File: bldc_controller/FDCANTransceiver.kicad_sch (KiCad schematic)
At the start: 4 parts, among them U4 TCAN1057AEVDRQ1

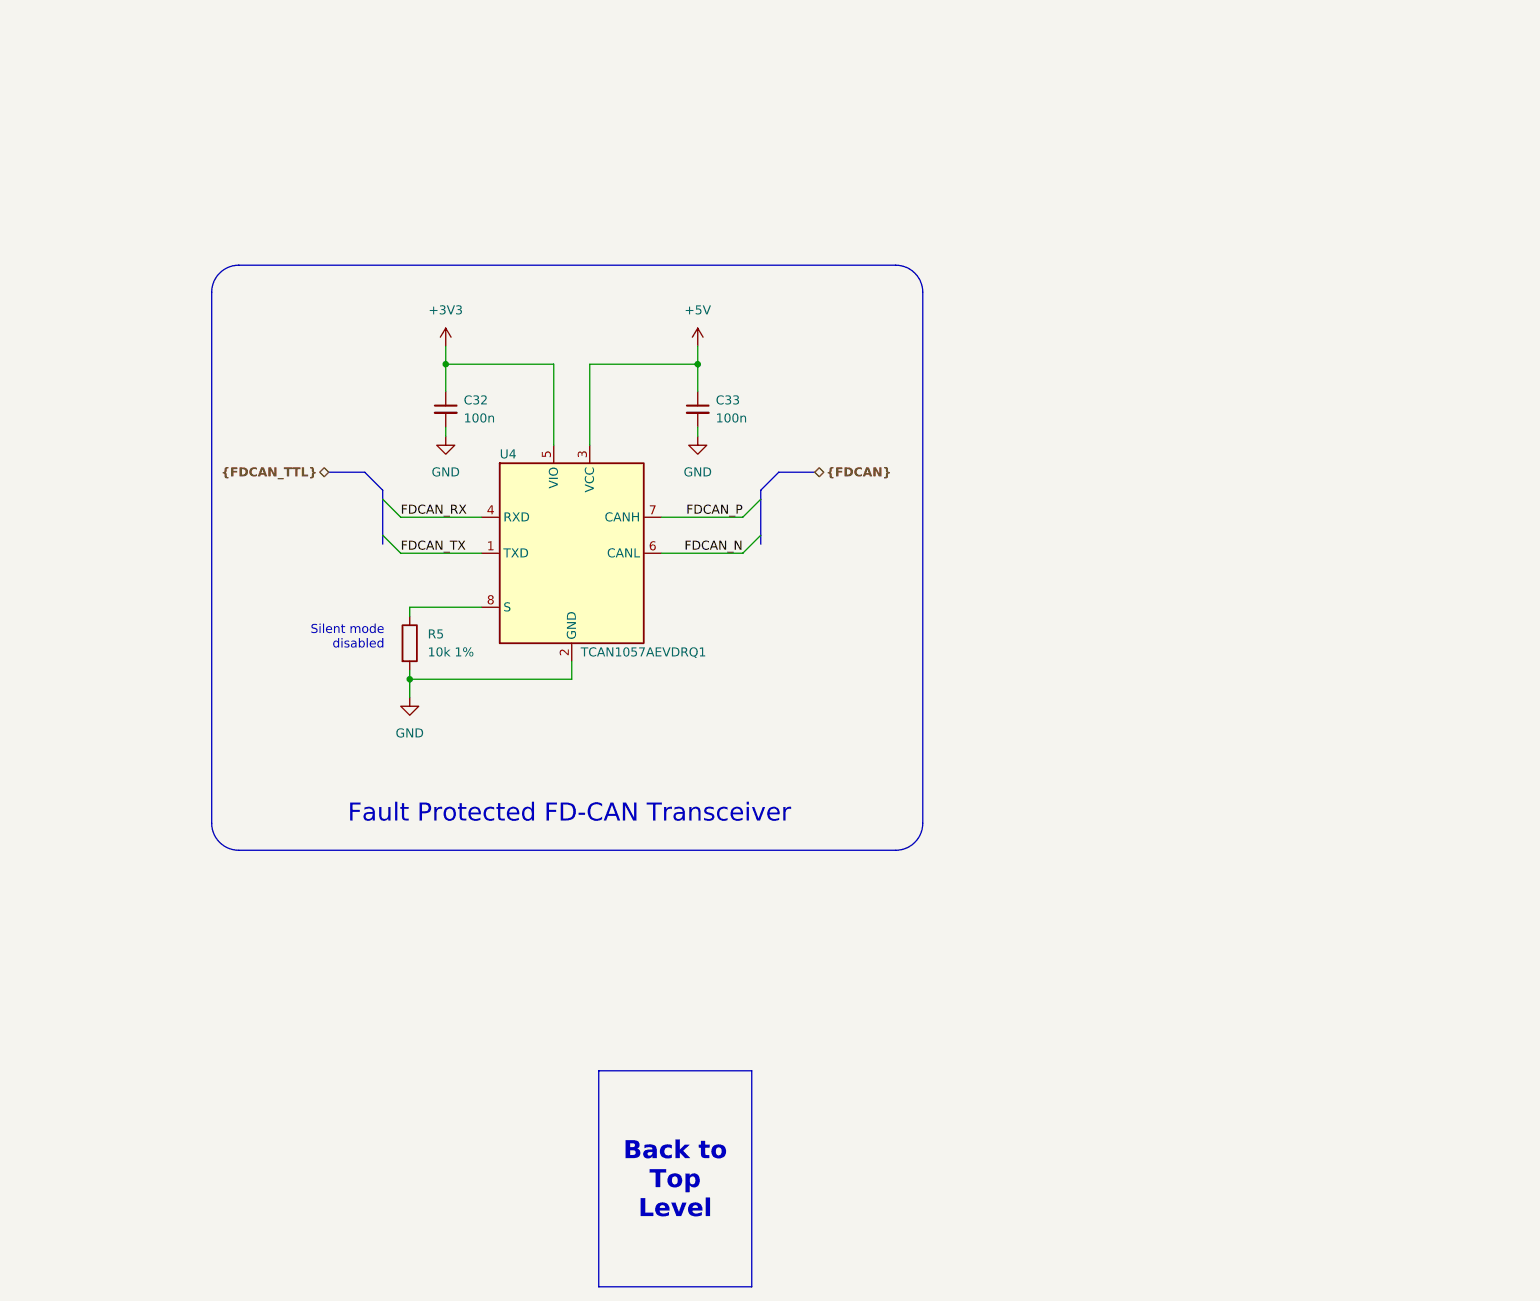
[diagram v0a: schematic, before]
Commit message: added temporary footprints and deleted extra files
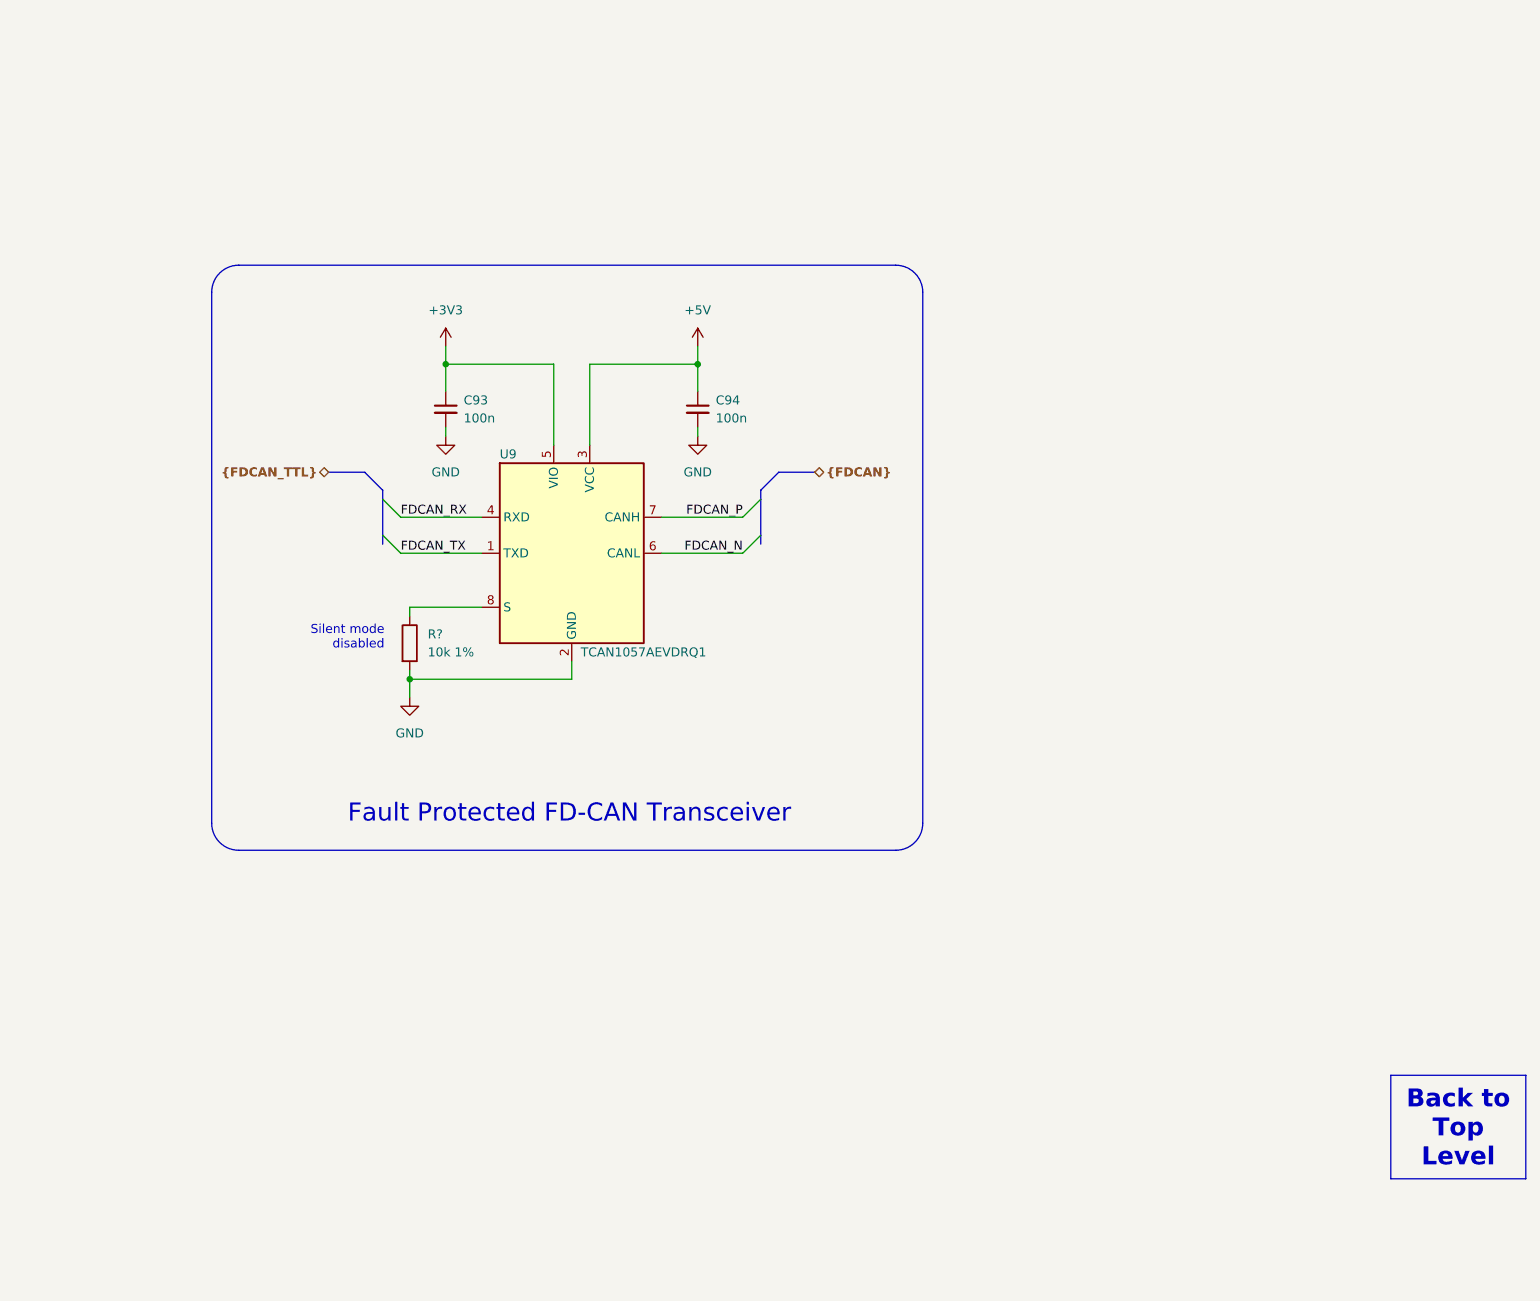
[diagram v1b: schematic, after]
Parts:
- C93: renamed from C32; footprint (none) -> Capacitor_SMD:C_0402_1005Metric
- C94: renamed from C33; footprint (none) -> Capacitor_SMD:C_0402_1005Metric
- R?: renamed from R5; footprint (none) -> Resistor_SMD:R_0402_1005Metric
- renumbered U4 to U9
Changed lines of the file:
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@@
   )
   (text_box "Back to Top Level"
-    (at 153.67 165.735 0) (size 21.59 30.48)
+    (at 265.43 166.37 0) (size 19.05 14.605)
     (stroke (width 0) (type default) (color 0 0 0 1))
     (fill (type color) (color 0 0 0 0.1))
@@
   (symbol (lib_id "power:+3V3") (at 132.08 63.5 0) (unit 1)
     (in_bom yes) (on_board yes) (dnp no) (fields_autoplaced)
-    (property "Reference" "#PWR043" (at 132.08 67.31 0)
+    (property "Reference" "#PWR054" (at 132.08 67.31 0)
       (effects (font (size 1.27 1.27)) hide)
     )
@@
       (project "bldc_controller"
         (path "/0650c7a8-acba-429c-9f8e-eec0baf0bc1c/926acdff-90be-4f7b-9e19-9f96ee9f0571"
-          (reference "#PWR043") (unit 1)
+          (reference "#PWR054") (unit 1)
         )
       )
@@
   (symbol (lib_id "power:GND") (at 127 113.03 0) (unit 1)
     (in_bom yes) (on_board yes) (dnp no) (fields_autoplaced)
-    (property "Reference" "#PWR042" (at 127 119.38 0)
+    (property "Reference" "#PWR053" (at 127 119.38 0)
       (effects (font (size 1.27 1.27)) hide)
     )
@@
       (project "bldc_controller"
         (path "/0650c7a8-acba-429c-9f8e-eec0baf0bc1c/926acdff-90be-4f7b-9e19-9f96ee9f0571"
-          (reference "#PWR042") (unit 1)
+          (reference "#PWR053") (unit 1)
         )
       )
@@
   (symbol (lib_id "power:GND") (at 132.08 76.2 0) (unit 1)
     (in_bom yes) (on_board yes) (dnp no) (fields_autoplaced)
-    (property "Reference" "#PWR044" (at 132.08 82.55 0)
+    (property "Reference" "#PWR055" (at 132.08 82.55 0)
       (effects (font (size 1.27 1.27)) hide)
     )
@@
       (project "bldc_controller"
         (path "/0650c7a8-acba-429c-9f8e-eec0baf0bc1c/926acdff-90be-4f7b-9e19-9f96ee9f0571"
-          (reference "#PWR044") (unit 1)
+          (reference "#PWR055") (unit 1)
         )
       )
@@
   (symbol (lib_id "power:GND") (at 167.64 76.2 0) (mirror y) (unit 1)
     (in_bom yes) (on_board yes) (dnp no) (fields_autoplaced)
-    (property "Reference" "#PWR046" (at 167.64 82.55 0)
+    (property "Reference" "#PWR057" (at 167.64 82.55 0)
       (effects (font (size 1.27 1.27)) hide)
     )
@@
       (project "bldc_controller"
         (path "/0650c7a8-acba-429c-9f8e-eec0baf0bc1c/926acdff-90be-4f7b-9e19-9f96ee9f0571"
-          (reference "#PWR046") (unit 1)
+          (reference "#PWR057") (unit 1)
         )
       )
@@
   (symbol (lib_id "Device:C_Small") (at 167.64 72.39 0) (unit 1)
     (in_bom yes) (on_board yes) (dnp no)
-    (property "Reference" "C33" (at 170.18 71.1263 0)
+    (property "Reference" "C94" (at 170.18 71.1263 0)
       (effects (font (size 1.27 1.27)) (justify left))
     )
@@
       (effects (font (size 1.27 1.27)) (justify left))
     )
-    (property "Footprint" "" (at 167.64 72.39 0)
+    (property "Footprint" "Capacitor_SMD:C_0402_1005Metric" (at 167.64 72.39 0)
       (effects (font (size 1.27 1.27)) hide)
     )
@@
       (project "bldc_controller"
         (path "/0650c7a8-acba-429c-9f8e-eec0baf0bc1c/926acdff-90be-4f7b-9e19-9f96ee9f0571"
-          (reference "C33") (unit 1)
+          (reference "C94") (unit 1)
         )
       )
@@
   (symbol (lib_id "power:+5V") (at 167.64 63.5 0) (unit 1)
     (in_bom yes) (on_board yes) (dnp no) (fields_autoplaced)
-    (property "Reference" "#PWR045" (at 167.64 67.31 0)
+    (property "Reference" "#PWR056" (at 167.64 67.31 0)
       (effects (font (size 1.27 1.27)) hide)
     )
@@
       (project "bldc_controller"
         (path "/0650c7a8-acba-429c-9f8e-eec0baf0bc1c/926acdff-90be-4f7b-9e19-9f96ee9f0571"
-          (reference "#PWR045") (unit 1)
+          (reference "#PWR056") (unit 1)
         )
       )
@@
   (symbol (lib_id "0_transceiver:TCAN1057AEVDRQ1") (at 149.86 92.71 0) (unit 1)
     (in_bom yes) (on_board yes) (dnp no)
-    (property "Reference" "U4" (at 139.7 78.74 0)
+    (property "Reference" "U9" (at 139.7 78.74 0)
       (effects (font (size 1.27 1.27)) (justify left))
     )
@@
       (project "bldc_controller"
         (path "/0650c7a8-acba-429c-9f8e-eec0baf0bc1c/926acdff-90be-4f7b-9e19-9f96ee9f0571"
-          (reference "U4") (unit 1)
+          (reference "U9") (unit 1)
         )
       )
@@
   (symbol (lib_id "Device:C_Small") (at 132.08 72.39 0) (unit 1)
     (in_bom yes) (on_board yes) (dnp no) (fields_autoplaced)
-    (property "Reference" "C32" (at 134.62 71.1263 0)
+    (property "Reference" "C93" (at 134.62 71.1263 0)
       (effects (font (size 1.27 1.27)) (justify left))
     )
@@
       (effects (font (size 1.27 1.27)) (justify left))
     )
-    (property "Footprint" "" (at 132.08 72.39 0)
+    (property "Footprint" "Capacitor_SMD:C_0402_1005Metric" (at 132.08 72.39 0)
       (effects (font (size 1.27 1.27)) hide)
     )
@@
       (project "bldc_controller"
         (path "/0650c7a8-acba-429c-9f8e-eec0baf0bc1c/926acdff-90be-4f7b-9e19-9f96ee9f0571"
-          (reference "C32") (unit 1)
+          (reference "C93") (unit 1)
         )
       )
@@
   (symbol (lib_id "Device:R") (at 127 105.41 0) (unit 1)
     (in_bom yes) (on_board yes) (dnp no) (fields_autoplaced)
-    (property "Reference" "R5" (at 129.54 104.14 0)
+    (property "Reference" "R?" (at 129.54 104.14 0)
       (effects (font (size 1.27 1.27)) (justify left))
     )
@@
       (effects (font (size 1.27 1.27)) (justify left))
     )
-    (property "Footprint" "" (at 125.222 105.41 90)
+    (property "Footprint" "Resistor_SMD:R_0402_1005Metric" (at 125.222 105.41 90)
       (effects (font (size 1.27 1.27)) hide)
     )
@@
       (project "bldc_controller"
         (path "/0650c7a8-acba-429c-9f8e-eec0baf0bc1c/ce1ea51b-4118-4fb5-9a41-40670da86eb7"
-          (reference "R5") (unit 1)
-        )
-        (path "/0650c7a8-acba-429c-9f8e-eec0baf0bc1c/926acdff-90be-4f7b-9e19-9f96ee9f0571"
-          (reference "R24") (unit 1)
-        )
-      )
+          (reference "R?") (unit 1)
+        )
+        (path "/0650c7a8-acba-429c-9f8e-eec0baf0bc1c/926acdff-90be-4f7b-9e19-9f96ee9f0571"
+          (reference "R29") (unit 1)
+        )
+      )
